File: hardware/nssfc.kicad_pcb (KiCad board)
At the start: 2 copper layers, 3 parts, among them U1 STM32F405RGTx, U2 W25Q128JVP, U3 QMC5883P

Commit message: worked on the schematic
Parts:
- added C1: 2.2u, Capacitor_SMD:C_0402_1005Metric, F.Cu at (207.6, 112.4)
- added C10: 1u, Capacitor_SMD:C_0402_1005Metric, F.Cu at (166.0, 107.1)
- added C11: 4.7u, Capacitor_SMD:C_0805_2012Metric, F.Cu at (163.9, 109.6)
- added C12: 100n, Capacitor_SMD:C_0402_1005Metric, F.Cu at (168.9, 99.2)
- added C13: 100n, Capacitor_SMD:C_0402_1005Metric, F.Cu at (168.9, 101.2)
- added C14: 100n, Capacitor_SMD:C_0402_1005Metric, F.Cu at (168.9, 103.2)
- added C15: 100n, Capacitor_SMD:C_0402_1005Metric, F.Cu at (168.9, 105.1)
- added C16: 2.2u, Capacitor_SMD:C_0402_1005Metric, F.Cu at (168.9, 107.1)
- added C17: 100n, Capacitor_SMD:C_0402_1005Metric, F.Cu at (171.7, 99.2)
- added C18: 10n, Capacitor_SMD:C_0402_1005Metric, F.Cu at (171.7, 101.2)
- added C19: 100n, Capacitor_SMD:C_0402_1005Metric, F.Cu at (196.9, 94.0)
- added C2: 2.2u, Capacitor_SMD:C_0402_1005Metric, F.Cu at (203.4, 123.7)
- added C20: 22u, Capacitor_SMD:C_0805_2012Metric, F.Cu at (163.9, 112.6)
- added C21: 10u, Capacitor_SMD:C_0805_2012Metric, F.Cu at (163.9, 115.6)
- added C22: 10u, Capacitor_SMD:C_0805_2012Metric, F.Cu at (163.9, 118.6)
- added C23: 100n, Capacitor_SMD:C_0402_1005Metric, F.Cu at (171.7, 105.1)
- added C24: 10u, Capacitor_SMD:C_0805_2012Metric, F.Cu at (163.9, 121.6)
- added C25: 100n, Capacitor_SMD:C_0402_1005Metric, F.Cu at (171.7, 107.1)
- added C3: 15p, Capacitor_SMD:C_0402_1005Metric, F.Cu at (163.1, 103.2)
- added C4: 15p, Capacitor_SMD:C_0402_1005Metric, F.Cu at (163.1, 105.1)
- added C5: 100n, Capacitor_SMD:C_0402_1005Metric, F.Cu at (163.1, 107.1)
- added C6: 100n, Capacitor_SMD:C_0402_1005Metric, F.Cu at (166.0, 99.2)
- added C7: 100n, Capacitor_SMD:C_0402_1005Metric, F.Cu at (166.0, 101.2)
- added C8: 100n, Capacitor_SMD:C_0402_1005Metric, F.Cu at (166.0, 103.2)
- added C9: 100n, Capacitor_SMD:C_0402_1005Metric, F.Cu at (166.0, 105.1)
- added D1: D_Schottky, Diode_SMD:D_SOD-123F, F.Cu at (206.6, 96.0)
- added D2: D_Schottky, Diode_SMD:D_SOD-123F, F.Cu at (150.0, 127.7)
- added J1: USB_C_Receptacle_USB2.0_16P, Connector_USB:USB_C_Receptacle_XKB_U262-16XN-4BVC11, F.Cu at (214.4, 101.8)
- added L1: 4.7u, Inductor_SMD:L_Changjiang_FNR4020S, F.Cu at (200.1, 93.9)
- added R1: 10k, Resistor_SMD:R_0402_1005Metric, F.Cu at (167.6, 109.1)
- added R2: 4.7k, Resistor_SMD:R_0402_1005Metric, F.Cu at (167.6, 111.1)
- added R3: 4.7k, Resistor_SMD:R_0402_1005Metric, F.Cu at (167.6, 113.1)
- added R4: 5.1k, Resistor_SMD:R_0402_1005Metric, F.Cu at (167.6, 115.0)
- added R5: 5.1k, Resistor_SMD:R_0402_1005Metric, F.Cu at (167.6, 117.0)
- added R6: 10k, Resistor_SMD:R_0402_1005Metric, F.Cu at (167.6, 119.0)
- added SW1: SW_Push, Button_Switch_SMD:SW_SPST_PTS810, F.Cu at (186.5, 107.3)
- added TP1: TestPoint, TestPoint:TestPoint_Pad_1.0x1.0mm, F.Cu at (163.2, 124.7)
- added TP2: TestPoint, TestPoint:TestPoint_Pad_1.0x1.0mm, F.Cu at (163.2, 127.7)
- added U4: ICM-20602, Package_LGA:LGA-16_3x3mm_P0.5mm_LayoutBorder3x5y, F.Cu at (190.3, 123.5)
- added U5: BMP580, Package_LGA:ST_HLGA-10_2x2mm_P0.5mm_LayoutBorder3x2y, F.Cu at (215.1, 121.6)
- added U6: AP63205WU, Package_TO_SOT_SMD:TSOT-23-6, F.Cu at (195.6, 96.1)
- added U7: TLV75733PDBV, Package_TO_SOT_SMD:SOT-23-5, F.Cu at (189.5, 95.4)
- added Y1: 25MHz, Crystal:Crystal_SMD_3225-4Pin_3.2x2.5mm, F.Cu at (189.8, 114.8)
- moved U2 64.0 mm to (202.8, 101.9), turned to -90 degrees
- moved U1 57.4 mm to (199.0, 115.7)
- moved U3 31.6 mm to (192.2, 102.7), turned to 180 degrees
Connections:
- U1 pad 17: unconnected-(U1-PA3-Pad17) -> /IMU_SPI_INT
- U1 pad 20: unconnected-(U1-PA4-Pad20) -> /IMU_SPI_CS
- U1 pad 21: unconnected-(U1-PA5-Pad21) -> /IMU_SPI_SCK
- U1 pad 22: unconnected-(U1-PA6-Pad22) -> /IMU_SPI_MISO
- U1 pad 23: unconnected-(U1-PA7-Pad23) -> /IMU_SPI_MOSI
- U1 pad 30: unconnected-(U1-PB11-Pad30) -> /BMP_SPI_INT
- U1 pad 33: unconnected-(U1-PB12-Pad33) -> /BMP_SPI_CSB
- U1 pad 34: unconnected-(U1-PB13-Pad34) -> /BMP_SPI_SCK
- U1 pad 35: unconnected-(U1-PB14-Pad35) -> /BMP_SPI_MISO
- U1 pad 36: unconnected-(U1-PB15-Pad36) -> /BMP_SPI_MOSI
- U1 pad 44: unconnected-(U1-PA11-Pad44) -> /USB_DN
- U1 pad 45: unconnected-(U1-PA12-Pad45) -> /USB_DP
- U1 pad 46: unconnected-(U1-PA13-Pad46) -> /~{F_SPI_WP}
- U1 pad 49: unconnected-(U1-PA14-Pad49) -> /~{F_SPI_RST}
- U1 pad 50: unconnected-(U1-PA15-Pad50) -> /~{F_SPI_CS}
- U1 pad 51: unconnected-(U1-PC10-Pad51) -> /F_SPI_CLK
- U1 pad 52: unconnected-(U1-PC11-Pad52) -> /F_SPI_MISO
- U1 pad 53: unconnected-(U1-PC12-Pad53) -> /F_SPI_MOSI
- U1 pad 58: unconnected-(U1-PB6-Pad58) -> /M_SDA
- U1 pad 59: unconnected-(U1-PB7-Pad59) -> /M_SCK
- U1 pad 60: unconnected-(U1-BOOT0-Pad60) -> Net-(U1-BOOT0)
- U1 pad 7: Net-(U1-NRST) -> /NRST
- U3 pad 1: unconnected-(U3-SCK-Pad1) -> /M_SCK
- U3 pad 10: unconnected-(U3-C1-Pad10) -> Net-(U3-C1)
- U3 pad 11: Net-(U3-GND-Pad11) -> GND
- U3 pad 16: unconnected-(U3-SDA-Pad16) -> /M_SDA
- U3 pad 2: unconnected-(U3-VDD-Pad2) -> +3V3
- U3 pad 9: Net-(U3-GND-Pad11) -> GND
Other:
- board outline added: 37 x 37 mm
- copper layers 2 -> 4

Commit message: worked on PCB layout
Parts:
- TP1, TP2: moved to B.Cu
- moved D2 63.5 mm to (204.0, 94.2), turned to 90 degrees
- moved C5 45.2 mm to (208.1, 111.3)
- moved C6 45.1 mm to (203.5, 124.4), turned to -90 degrees
- moved R5 43.3 mm to (208.7, 103.3), turned to 180 degrees
- moved R4 43.1 mm to (208.1, 100.3), turned to 180 degrees
- moved C7 37.9 mm to (196.0, 124.3), turned to -90 degrees
- moved C24 37.5 mm to (188.3, 93.1), turned to 180 degrees
- moved C20 35.3 mm to (193.4, 93.1), turned to 180 degrees
- moved C21 33.1 mm to (192.2, 98.5), turned to -90 degrees
- moved C22 32.8 mm to (184.7, 93.3), turned to 180 degrees
- moved R6 31.2 mm to (196.7, 107.8), turned to 180 degrees
- moved R3 29.4 mm to (195.5, 103.6), turned to -90 degrees
- moved C4 29.2 mm to (190.0, 116.4), turned to 180 degrees
- moved C3 28.2 mm to (190.1, 111.2)
- moved R2 26.3 mm to (193.3, 105.5)
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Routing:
- net /USB_DN: track 0.00 -> 22.4 mm
- net /USB_DP: track 0.00 -> 22.4 mm
- net /BMP_SPI_INT: track 0.00 -> 14.2 mm
- net /BMP_SPI_SCK: track 0.00 -> 13.9 mm, vias 0 -> 2
- net /BMP_SPI_MOSI: track 0.00 -> 11.8 mm
- net /BMP_SPI_MISO: track 0.00 -> 10.9 mm
- net /BMP_SPI_CSB: track 0.00 -> 10.5 mm
- net +3V3: track 0.00 -> 8.58 mm
- net /PH0: track 0.00 -> 6.24 mm
- net /PH1: track 0.00 -> 3.51 mm
- net Net-(U1-VCAP_2): track 0.00 -> 2.93 mm
- net /~{F_SPI_WP}: track 0.00 -> 2.85 mm, vias 0 -> 2
- net Net-(U1-VCAP_1): track 0.00 -> 2.57 mm
- net Net-(U1-BOOT0): track 0.00 -> 2.26 mm
- net /NRST: track 0.00 -> 1.81 mm, vias 0 -> 1
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
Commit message: completed PCB
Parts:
- moved C12 53.6 mm to (216.0, 124.8), turned to -90 degrees
- moved C13 51.8 mm to (215.0, 124.8), turned to -90 degrees
- moved C14 36.5 mm to (205.2, 106.3)
- moved C10 32.9 mm to (193.7, 124.7)
- moved C16 31.0 mm to (193.7, 125.7)
- moved C8 27.2 mm to (192.3, 110.0), turned to 180 degrees
- moved C15 26.9 mm to (187.4, 124.6), turned to 180 degrees
- moved C9 26.6 mm to (192.3, 109.0), turned to 180 degrees
- moved C18 25.4 mm to (190.9, 117.9), turned to 180 degrees
- moved C17 13.4 mm to (184.3, 103.9), turned to 90 degrees
- moved C7 4.02 mm to (193.2, 121.5), turned to 180 degrees
- moved C3 0.88 mm to (190.1, 110.4)
- moved R6 0.50 mm to (196.7, 108.3)
- moved C4 0.50 mm to (189.5, 116.4)
- moved Y1 0.50 mm to (189.6, 113.8)
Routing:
- net +3V3: track 8.58 -> 135.1 mm, vias 0 -> 7
- net +5V: track 0.00 -> 28.4 mm, vias 0 -> 2
- net /~{F_SPI_WP}: track 2.85 -> 19.1 mm
- net /NRST: track 1.81 -> 17.8 mm, vias 1 -> 2
- net GND: track 0.00 -> 15.0 mm, vias 1 -> 13
- net Net-(U1-BOOT0): track 2.26 -> 15.3 mm
- net /M_SDA: track 0.00 -> 12.5 mm, vias 0 -> 2
- net Net-(D2-A): track 0.00 -> 12.0 mm
- net /~{F_SPI_CS}: track 0.00 -> 11.9 mm, vias 0 -> 2
- net /F_SPI_MISO: track 0.00 -> 11.9 mm, vias 0 -> 2
- net Net-(D1-A): track 0.00 -> 11.4 mm
- net /IMU_SPI_MISO: track 0.00 -> 10.7 mm, vias 0 -> 2
- net /IMU_SPI_MOSI: track 0.00 -> 9.95 mm, vias 0 -> 2
- net /M_SCK: track 0.00 -> 9.14 mm
- net /IMU_SPI_SCK: track 0.00 -> 7.38 mm
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- added copper zone on B.Cu, net GND
- added copper zone on F.Cu, net GND

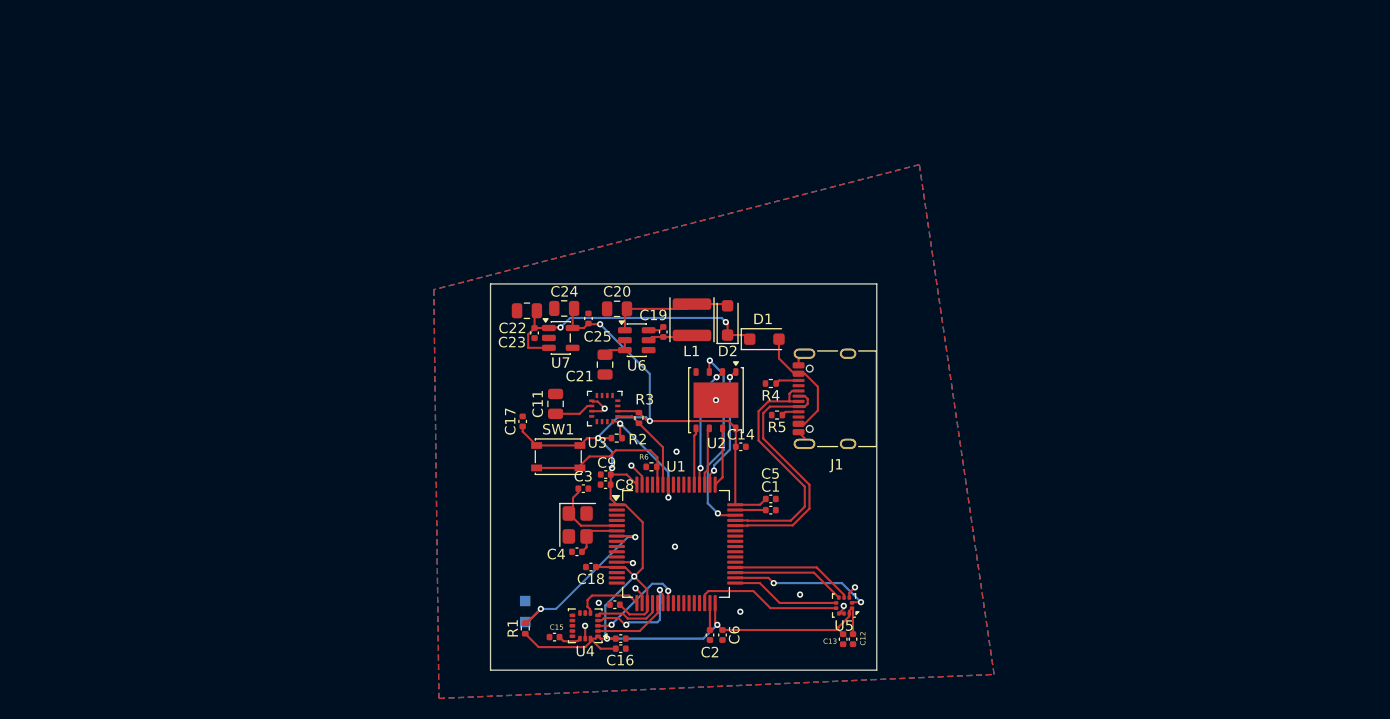
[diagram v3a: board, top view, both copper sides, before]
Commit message: layout change in PCB
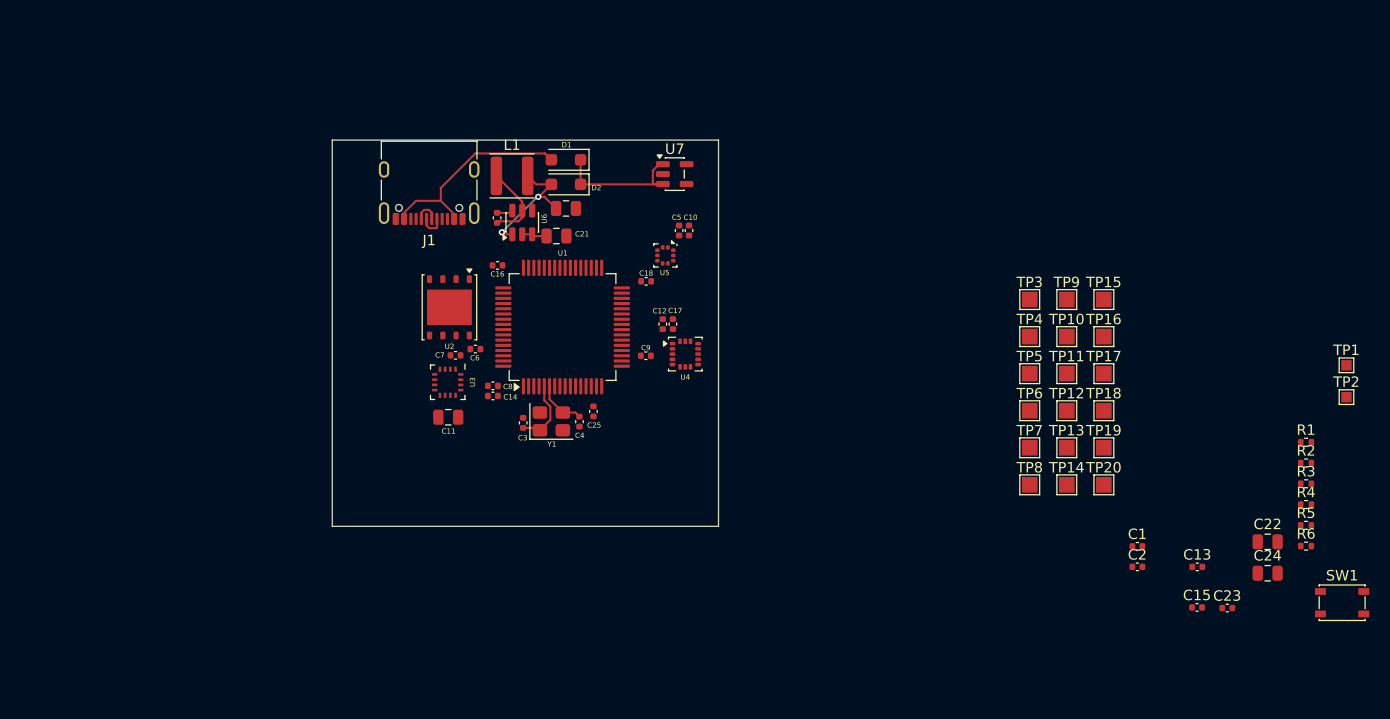
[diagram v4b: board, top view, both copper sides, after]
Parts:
- added TP10: TestPoint, TestPoint:TestPoint_Pad_1.5x1.5mm, F.Cu at (236.5, 95.8)
- added TP11: TestPoint, TestPoint:TestPoint_Pad_1.5x1.5mm, F.Cu at (236.5, 99.3)
- added TP12: TestPoint, TestPoint:TestPoint_Pad_1.5x1.5mm, F.Cu at (236.5, 102.9)
- added TP13: TestPoint, TestPoint:TestPoint_Pad_1.5x1.5mm, F.Cu at (236.5, 106.4)
- added TP14: TestPoint, TestPoint:TestPoint_Pad_1.5x1.5mm, F.Cu at (236.5, 110.0)
- added TP15: TestPoint, TestPoint:TestPoint_Pad_1.5x1.5mm, F.Cu at (240.0, 92.2)
- added TP16: TestPoint, TestPoint:TestPoint_Pad_1.5x1.5mm, F.Cu at (240.0, 95.8)
- added TP17: TestPoint, TestPoint:TestPoint_Pad_1.5x1.5mm, F.Cu at (240.0, 99.3)
- added TP18: TestPoint, TestPoint:TestPoint_Pad_1.5x1.5mm, F.Cu at (240.0, 102.9)
- added TP19: TestPoint, TestPoint:TestPoint_Pad_1.5x1.5mm, F.Cu at (240.0, 106.4)
- added TP20: TestPoint, TestPoint:TestPoint_Pad_1.5x1.5mm, F.Cu at (240.0, 110.0)
- added TP3: TestPoint, TestPoint:TestPoint_Pad_1.5x1.5mm, F.Cu at (232.9, 92.2)
- added TP4: TestPoint, TestPoint:TestPoint_Pad_1.5x1.5mm, F.Cu at (232.9, 95.8)
- added TP5: TestPoint, TestPoint:TestPoint_Pad_1.5x1.5mm, F.Cu at (232.9, 99.3)
- added TP6: TestPoint, TestPoint:TestPoint_Pad_1.5x1.5mm, F.Cu at (232.9, 102.9)
- added TP7: TestPoint, TestPoint:TestPoint_Pad_1.5x1.5mm, F.Cu at (232.9, 106.4)
- added TP8: TestPoint, TestPoint:TestPoint_Pad_1.5x1.5mm, F.Cu at (232.9, 110.0)
- added TP9: TestPoint, TestPoint:TestPoint_Pad_1.5x1.5mm, F.Cu at (236.5, 92.2)
- TP1, TP2: moved to F.Cu
- moved TP1 81.9 mm to (263.2, 98.5), turned to 0 degrees
- moved TP2 81.6 mm to (263.2, 101.6), turned to 0 degrees
- moved R1 76.9 mm to (259.4, 105.9), turned to 0 degrees
- moved SW1 76.4 mm to (262.8, 121.3)
- moved C22 74.3 mm to (255.7, 115.5), turned to 0 degrees
- moved C24 72.0 mm to (255.7, 118.5), turned to 0 degrees
- moved C23 71.4 mm to (251.8, 121.8), turned to 0 degrees
- moved R2 66.1 mm to (259.4, 107.9)
- moved R3 64.2 mm to (259.4, 109.9), turned to 0 degrees
- moved R6 63.2 mm to (259.4, 115.9), turned to 0 degrees
- moved C15 61.6 mm to (248.9, 121.7), turned to 0 degrees
- moved R4 52.6 mm to (259.4, 111.9), turned to 0 degrees
- moved R5 51.8 mm to (259.4, 113.9), turned to 0 degrees
- moved J1 44.3 mm to (175.4, 80.9), turned to 180 degrees
- moved C2 41.5 mm to (243.2, 117.9), turned to 0 degrees
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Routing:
- net +3V3: track 135.1 -> 0.00 mm, vias 7 -> 0
- net /USB_DN: track 24.8 -> 2.58 mm
- net /USB_DP: track 24.2 -> 2.45 mm
- net /~{F_SPI_WP}: track 19.1 -> 0.00 mm, vias 2 -> 0
- net /NRST: track 17.8 -> 0.00 mm, vias 2 -> 0
- net +5V: track 28.4 -> 12.9 mm, vias 2 -> 0
- net Net-(U1-BOOT0): track 15.3 -> 0.00 mm
- net GND: track 15.0 -> 0.00 mm, vias 13 -> 0
- net /BMP_SPI_INT: track 14.2 -> 0.00 mm
- net /BMP_SPI_SCK: track 13.9 -> 0.00 mm, vias 2 -> 0
- net /M_SDA: track 12.5 -> 0.00 mm, vias 2 -> 0
- net /~{F_SPI_CS}: track 11.9 -> 0.00 mm, vias 2 -> 0
- net /F_SPI_MISO: track 11.9 -> 0.00 mm, vias 2 -> 0
- net /BMP_SPI_MOSI: track 11.8 -> 0.00 mm
- net /BMP_SPI_MISO: track 10.9 -> 0.00 mm
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- removed copper zone on B.Cu, net GND
- removed copper zone on F.Cu, net GND

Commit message: rerouted PCB
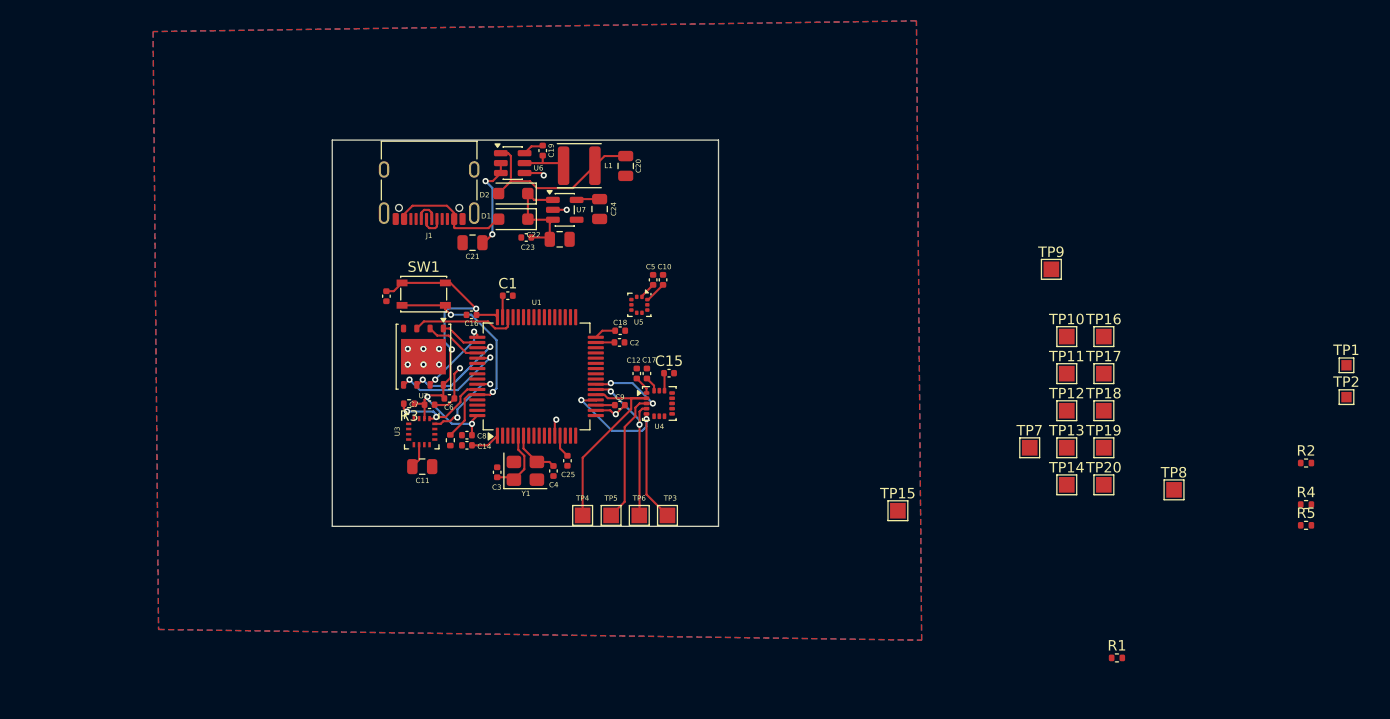
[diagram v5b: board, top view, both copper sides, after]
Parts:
- moved SW1 92.8 mm to (174.8, 91.7)
- moved R3 86.3 mm to (173.4, 102.2), turned to 180 degrees
- moved R6 82.6 mm to (177.4, 105.7), turned to -90 degrees
- moved C13 81.9 mm to (171.3, 91.9), turned to -90 degrees
- moved C23 76.0 mm to (184.7, 86.3), turned to 180 degrees
- moved C22 73.8 mm to (187.9, 86.5)
- moved C24 72.9 mm to (191.7, 83.6), turned to -90 degrees
- moved C1 64.9 mm to (182.9, 91.9)
- moved C15 55.3 mm to (198.3, 99.3)
- moved C2 54.1 mm to (193.6, 96.3)
- moved TP4 46.1 mm to (190.1, 112.9)
- moved TP5 42.3 mm to (192.8, 112.9)
- moved TP3 40.4 mm to (198.2, 112.9)
- moved TP6 38.7 mm to (195.5, 112.9)
- moved TP15 28.3 mm to (220.3, 112.5)
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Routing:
- net +3V3: track 0.00 -> 55.5 mm, vias 0 -> 4
- net Net-(U1-BOOT0): track 0.00 -> 22.8 mm, vias 0 -> 2
- net /IMU_SPI_CS: track 0.00 -> 20.4 mm, vias 0 -> 2
- net /IMU_SPI_SCK: track 0.00 -> 19.6 mm
- net /IMU_SPI_MOSI: track 0.00 -> 19.4 mm, vias 0 -> 2
- net /IMU_SPI_MISO: track 0.00 -> 16.6 mm, vias 0 -> 2
- net GND: track 0.00 -> 13.4 mm, vias 0 -> 11
- net /F_SPI_MOSI: track 0.00 -> 11.5 mm, vias 0 -> 2
- net /F_SPI_CLK: track 0.00 -> 10.3 mm, vias 0 -> 2
- net /M_SCK: track 0.00 -> 10.3 mm, vias 0 -> 2
- net /~{F_SPI_WP}: track 0.00 -> 10.3 mm
- net /M_SDA: track 0.00 -> 8.60 mm, vias 0 -> 2
- net Net-(D1-A): track 20.3 -> 12.0 mm
- net /~{F_SPI_RST}: track 0.00 -> 7.50 mm, vias 0 -> 2
- net VBUS: track 2.40 -> 9.38 mm, vias 0 -> 2
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- added copper zone on B.Cu, net GND
- added copper zone on F.Cu, net GND
